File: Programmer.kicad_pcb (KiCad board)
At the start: 2 copper layers, 76.2 x 50.8 mm, 63 parts, among them CON1 USB_OTG, M1 ESP-12E, P1 CONN_01X12, P3 CONN_12, Q1 MMBT3904, Q2 MMBT3906, Q3 MMBT3904, Q4 BSS84, Q5 BSS138L, Q6 MMBT3904, Q7 MMBT3904, SW1 Upload, SW2 RESET, U1 AP2112K-3.3, U10 NC7SB3157, U2 23LC1024, U3 FXMA108, U8 CH340G, Y1 12 Mhz

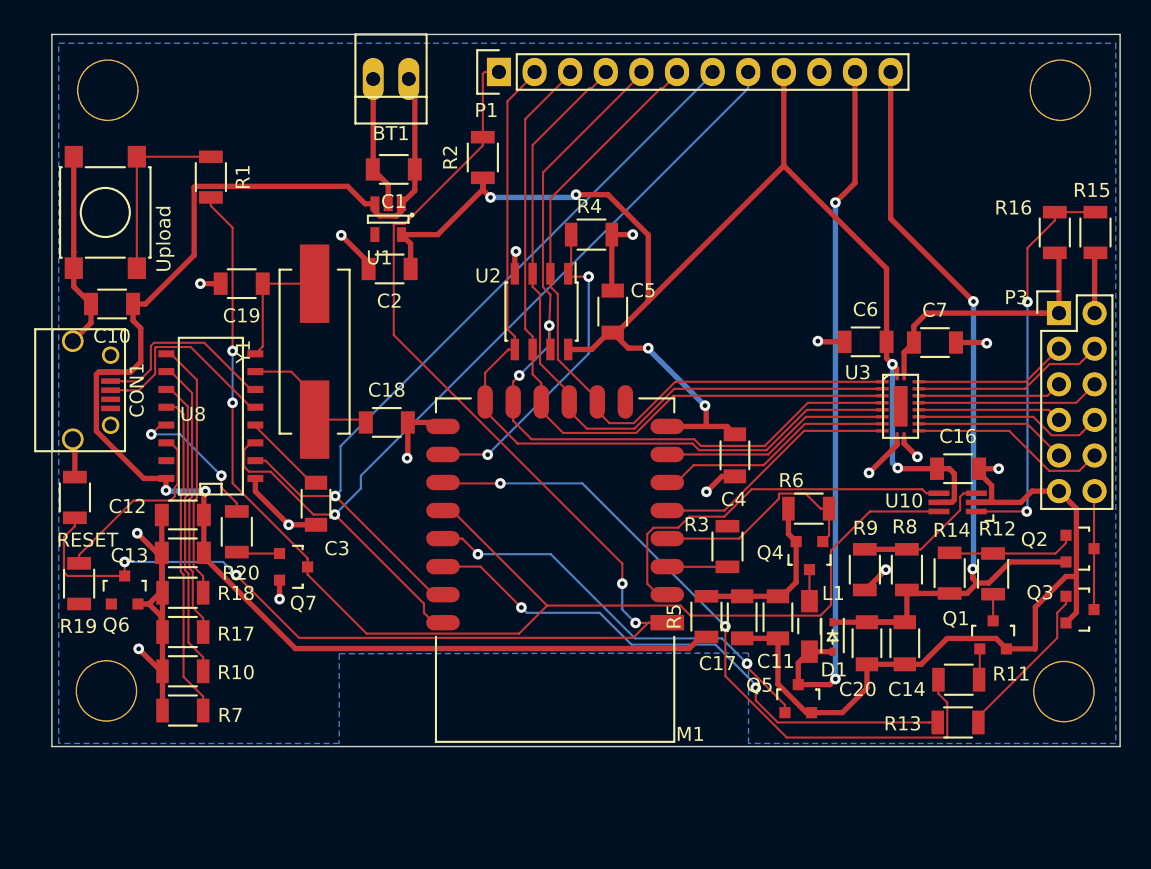
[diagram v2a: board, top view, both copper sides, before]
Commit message: New Layout V00E
Updated layout with newest schematic design.
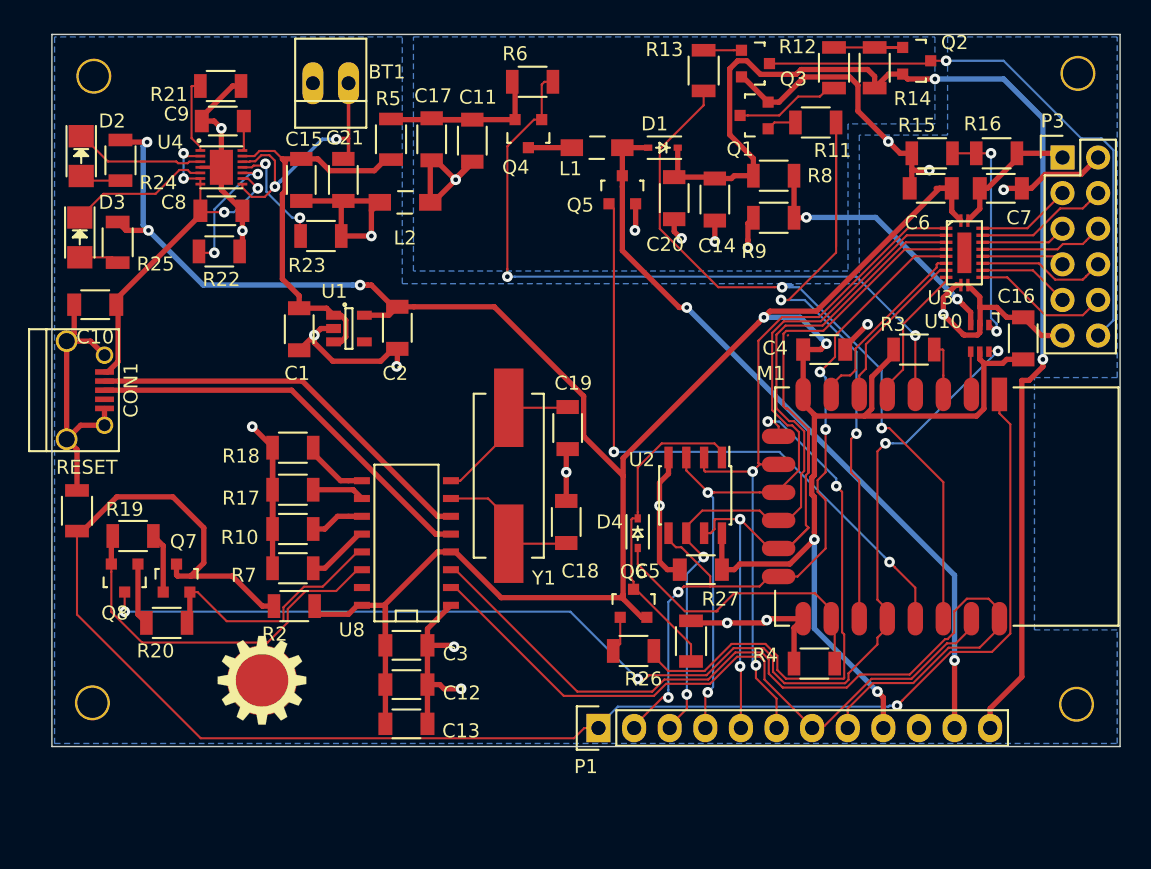
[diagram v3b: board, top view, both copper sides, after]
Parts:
- removed R1: 10K, Resistors_SMD:R_1206
- removed the REF** at (122.8, 40.3)
- removed the REF** at (123.0, 83.2)
- removed the REF** at (54.7, 83.2)
- removed the REF** at (54.8, 40.3)
- removed SW2: RESET, Resistors_SMD:R_1206
- added C15: 1 µF, Capacitors_SMD:C_1206, F.Cu at (68.6, 46.7)
- added C21: 10 µF, Capacitors_SMD:C_1206, F.Cu at (71.6, 46.7)
- added C8: 1 µF, Capacitors_SMD:C_1206, F.Cu at (62.9, 48.9)
- added C9: 0.1 uF, Capacitors_SMD:C_1206, F.Cu at (63.0, 42.5)
- added D2: Red, LEDs:LED_1206, F.Cu at (52.9, 45.0)
- added D3: Green, LEDs:LED_1206, F.Cu at (52.8, 50.8)
- added D4: SD103, Diodes_SMD:SOD-323, F.Cu at (92.6, 71.9)
- added G***: LOGO, UprogrammerFPs:LogoSilk, F.Cu at (65.8, 82.4)
- added G***: LOGO, UprogrammerFPs:LogoMask, F.Cu at (65.8, 82.4)
- added L2: 2.2 µH, Choke_SMD:Choke_SMD_1206_Standard, F.Cu at (76.0, 48.3)
- added Q8: MMBT3904, TO_SOT_Packages_SMD:SOT-23, F.Cu at (56.0, 75.1)
- added R21: 150K, Resistors_SMD:R_1206, F.Cu at (62.9, 40.0)
- added R22: 100K, Resistors_SMD:R_1206, F.Cu at (62.8, 51.8)
- added R23: 10K, Resistors_SMD:R_1206, F.Cu at (70.0, 50.7)
- added R24: 200, Resistors_SMD:R_1206, F.Cu at (55.7, 45.3)
- added R25: 200, Resistors_SMD:R_1206, F.Cu at (55.5, 51.1)
- added R26: 100K, Resistors_SMD:R_1206, F.Cu at (92.3, 80.3)
- added R27: 22K, Resistors_SMD:R_1206, F.Cu at (96.4, 79.6)
- added REF**: MountingHole_2-5mm, Mounting_Holes:MountingHole_2-5mm, F.Cu at (124.0, 39.1)
- added REF**: MountingHole_2-5mm, Mounting_Holes:MountingHole_2-5mm, F.Cu at (123.9, 84.1)
- added REF**: MountingHole_2-5mm, Mounting_Holes:MountingHole_2-5mm, F.Cu at (53.7, 84.0)
- added REF**: MountingHole_2-5mm, Mounting_Holes:MountingHole_2-5mm, F.Cu at (53.8, 39.3)
- added U4: AAT3672-4.2-1, UprogrammerFPs:DFN-14-1EP_3x3mm_Pitch0.4mm, F.Cu at (62.9, 45.9)
- BT1: value BATTERY -> LiPo
- Q1: value MMBT3904 -> BSS138L; footprint Housings_SOT-23_SOT-143_TSOT-6:SOT-23 -> TO_SOT_Packages_SMD:SOT-23
- Q2, Q3, Q4, Q5, Q7: footprint Housings_SOT-23_SOT-143_TSOT-6:SOT-23 -> TO_SOT_Packages_SMD:SOT-23
- Q6: value MMBT3904 -> MMBT3906; footprint Housings_SOT-23_SOT-143_TSOT-6:SOT-23 -> TO_SOT_Packages_SMD:SOT-23
- R4: value 10K -> 22K
- R5: value 10 -> 1K
- R8: value 58.2K -> 100K
- SW1: value Upload -> RESET; footprint Buttons_Switches_SMD:SW_SPST_PTS645 -> Resistors_SMD:R_1206
- U1: footprint Housings_SOT-23_SOT-143_TSOT-6:SOT-23-5 -> TO_SOT_Packages_SMD:SOT-23-5
- U10: footprint Housings_SOT-23_SOT-143_TSOT-6:SC-70-6_Handsoldering -> TO_SOT_Packages_SMD:SC-70-6
- moved R13 49.9 mm to (97.3, 38.9), turned to 270 degrees
- moved P1 47.3 mm to (89.8, 85.8)
- moved Q3 45.3 mm to (101.0, 38.4)
- moved R11 41.0 mm to (105.3, 42.6), turned to 0 degrees
- moved R5 40.8 mm to (75.0, 43.8)
- moved Q1 40.8 mm to (100.9, 42.1), turned to 90 degrees
- moved C17 40.7 mm to (77.9, 43.8)
- moved C11 40.4 mm to (80.8, 43.9)
- moved Q5 38.4 mm to (91.5, 47.4)
- moved R12 37.8 mm to (106.6, 38.7)
- moved L1 37.4 mm to (89.7, 44.4), turned to 0 degrees
- moved D1 36.9 mm to (94.4, 44.4), turned to 180 degrees
- moved Q2 36.7 mm to (112.5, 38.2)
- moved R14 36.4 mm to (109.5, 38.7)
- moved Q6 36.3 mm to (92.3, 76.9)
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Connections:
- BT1 pad 1: +BATT -> Net-(BT1-Pad1)
- C10 pad 1: +BATT -> +5V
- C11 pad 2: GND -> /GNDpp
- C12 pad 1: +BATT -> 3V3
- C13 pad 1: +BATT -> 3V3
- C14 pad 2: GND -> /GNDpp
- C17 pad 2: GND -> /GNDpp
- C20 pad 2: GND -> /GNDpp
- C3 pad 1: Net-(C3-Pad1) -> 3V3
- C5 pad 1: 3V3 -> GND
- C5 pad 2: GND -> 3V3
- CON1 pad 1: +BATT -> +5V
- M1 pad 16: Net-(M1-Pad16) -> /MTDO
- Q5 pad 2: GND -> /GNDpp
- Q6 pad 2: GND -> 3V3
- Q6 pad 3: /~RST -> Net-(D4-Pad1)
- Q7 pad 2: GND -> Net-(Q7-Pad2)
- Q7 pad 3: Net-(M1-Pad18) -> /~RST
- R19 pad 1: Net-(Q6-Pad1) -> Net-(Q7-Pad1)
- R20 pad 1: Net-(Q7-Pad1) -> Net-(Q8-Pad1)
- R20 pad 2: Net-(R20-Pad2) -> Net-(Q7-Pad2)
- R4 pad 2: Net-(M1-Pad16) -> /MTDO
- R9 pad 2: GND -> /GNDpp
- SW1 pad 1: Net-(R1-Pad1) -> GND
- SW1 pad 2: GND -> /~RST
- U2 pad 1: Net-(M1-Pad16) -> Net-(D4-Pad1)
- U8 pad 13: Net-(R20-Pad2) -> Net-(Q7-Pad2)
- U8 pad 16: +BATT -> 3V3
- U8 pad 4: Net-(C3-Pad1) -> 3V3
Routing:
- net 3V3: track 105.4 -> 212.5 mm, vias 6 -> 7
- net +BATT: track 102.5 -> 28.9 mm, vias 2 -> 0
- net Net-(M1-Pad9): track 0.00 -> 39.5 mm, vias 0 -> 2
- net /~HV: track 16.0 -> 51.0 mm, vias 0 -> 2
- net Net-(P3-Pad12): track 8.47 -> 40.9 mm, vias 0 -> 1
- net +5V: track 0.00 -> 27.4 mm, vias 0 -> 4
- net VPP: track 61.7 -> 87.5 mm
- net Net-(M1-Pad2): track 27.5 -> 3.07 mm
- net Net-(D4-Pad1): track 0.00 -> 23.5 mm
- net Net-(M1-Pad16): track 23.3 -> 0.00 mm, vias 2 -> 0
- net /MTDO: track 0.00 -> 21.4 mm
- net Net-(BT1-Pad1): track 0.00 -> 19.9 mm, vias 0 -> 2
- net Net-(R7-Pad2): track 23.3 -> 4.48 mm
- net /GNDpp: track 0.00 -> 18.5 mm, vias 0 -> 5
- net Net-(Q7-Pad2): track 0.00 -> 18.0 mm
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- added copper zone on B.Cu, net /GNDpp

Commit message: Hardware V00F
BOM and Fabrication files
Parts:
- removed G***: LOGO, UprogrammerFPs:LogoSilk
- removed G***: LOGO, UprogrammerFPs:LogoMask
- added Ref**: Val**, UprogrammerFPs:PILogo, F.Cu at (62.9, 83.1)

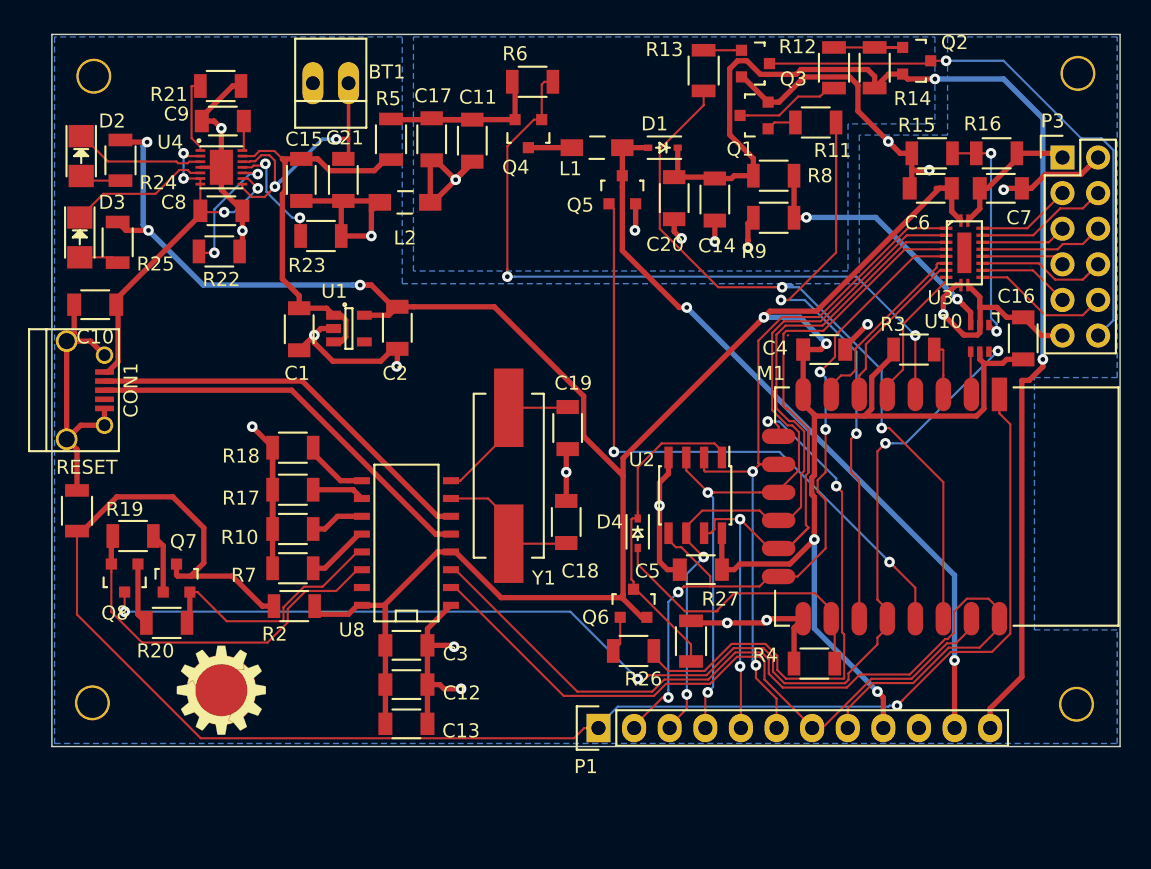
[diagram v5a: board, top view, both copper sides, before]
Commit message: Hardware Version 00H
Schematic updated to get ready for a new layout.
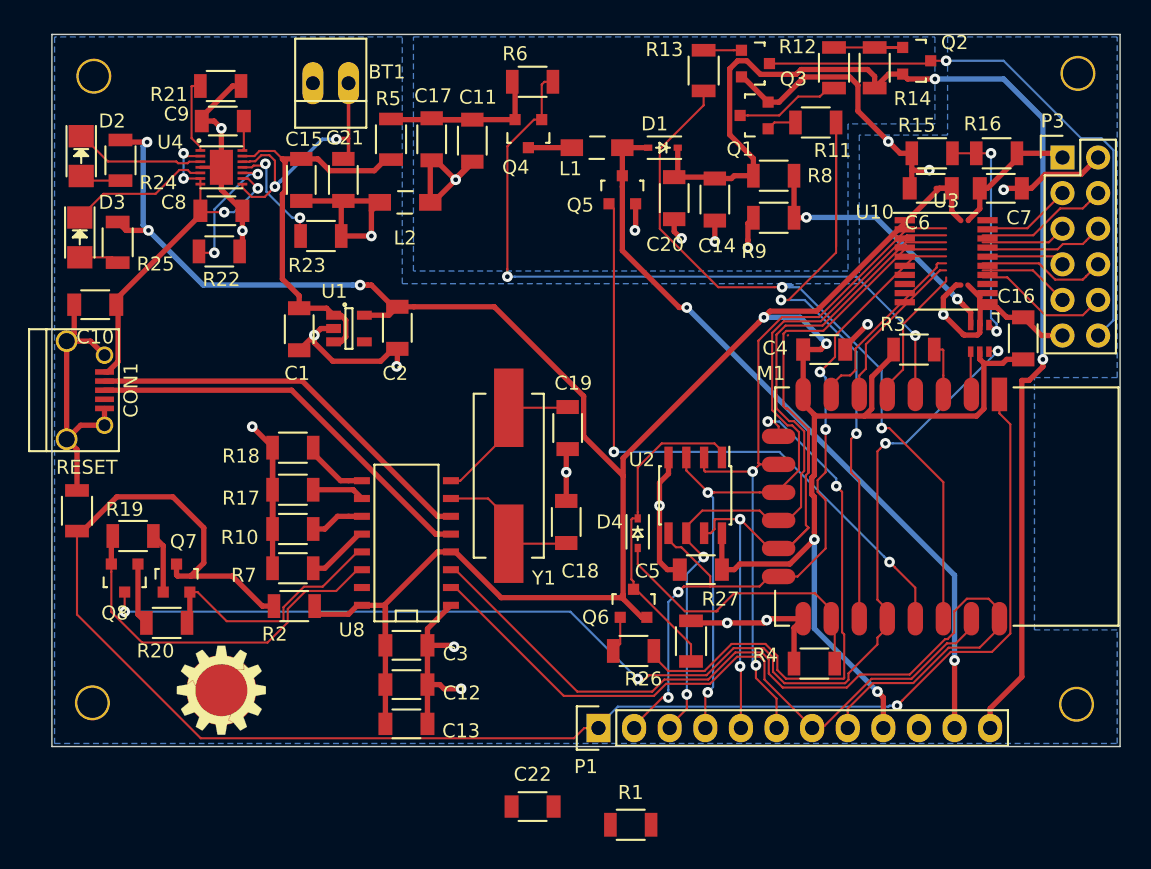
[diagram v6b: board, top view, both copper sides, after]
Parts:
- added C22: 0.1 µF, Capacitors_SMD:C_1206, F.Cu at (85.1, 91.4)
- added R1: 100k, Resistors_SMD:R_1206, F.Cu at (92.1, 92.7)
- R5: value 1K -> 47
- U3: value FXMA108 -> TXS0108EPWR; footprint Uprogrammer FPs:DQFN20 -> Housings_SSOP:TSSOP-20_4.4x6.5mm_Pitch0.65mm
- moved U3 1.43 mm to (114.6, 52.5)
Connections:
- C11 pad 2: /GNDpp -> GND
- C14 pad 2: /GNDpp -> GND
- C17 pad 2: /GNDpp -> GND
- C20 pad 2: /GNDpp -> GND
- CON1 pad 4: Net-(CON1-Pad4) -> (no net)
- D4 pad 2: /MTDO -> (no net)
- M1 pad 11: /IO2 -> /IO3
- M1 pad 12: /SCK -> /IO2
- M1 pad 13: /IO3 -> /MOSI
- M1 pad 14: /MOSI -> /SCLK
- M1 pad 16: /MTDO -> /A_SEL
- P1 pad 3: /SCK -> (no net)
- Q5 pad 2: /GNDpp -> GND
- R4 pad 2: /MTDO -> /A_SEL
- R9 pad 2: /GNDpp -> GND
- U10 pad 6: Net-(M1-Pad18) -> /A_SEL
- U2 pad 1: Net-(D4-Pad1) -> Net-(M1-Pad18)
- U2 pad 6: /SCK -> /SCLK
- U3 pad 1: 3V3 -> /MISO
- U3 pad 10: GND -> Net-(C22-Pad1)
- U3 pad 11: GND -> (no net)
- U3 pad 19: Net-(P3-Pad3) -> VEE
- U3 pad 2: /MISO -> 3V3
- U3 pad 20: VEE -> Net-(P3-Pad3)
- U3 pad 3: /IO2 -> /IO3
- U3 pad 4: /SCK -> /IO2
- U3 pad 5: /IO3 -> /MOSI
- U3 pad 6: /MOSI -> /SCLK
- U8 pad 15: Net-(U8-Pad15) -> (no net)
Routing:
- net /SCK: track 54.1 -> 0.00 mm, vias 2 -> 0
- net /IO2: track 54.7 -> 89.3 mm
- net /SCLK: track 0.00 -> 32.3 mm, vias 0 -> 3
- net /A_SEL: track 0.00 -> 22.1 mm, vias 0 -> 1
- net /MTDO: track 21.4 -> 0.00 mm
- net 3V3: track 212.5 -> 229.2 mm
- net /MISO: track 51.7 -> 35.0 mm
- net GND: track 168.3 -> 181.4 mm, vias 17 -> 22
- net /GNDpp: track 18.5 -> 5.38 mm, vias 5 -> 0
- net /IO3: track 60.4 -> 49.5 mm
- net Net-(D4-Pad1): track 23.5 -> 12.9 mm
- net Net-(M1-Pad18): track 87.6 -> 97.6 mm, vias 4 -> 3
- net Net-(P3-Pad10): track 9.81 -> 1.22 mm
- net Net-(P3-Pad5): track 6.10 -> 13.7 mm
- net VEE: track 9.93 -> 13.1 mm
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
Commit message: New Layout Hardware V00I
Updated layout to match schematic in Version H. Ready to go to
fabrication.
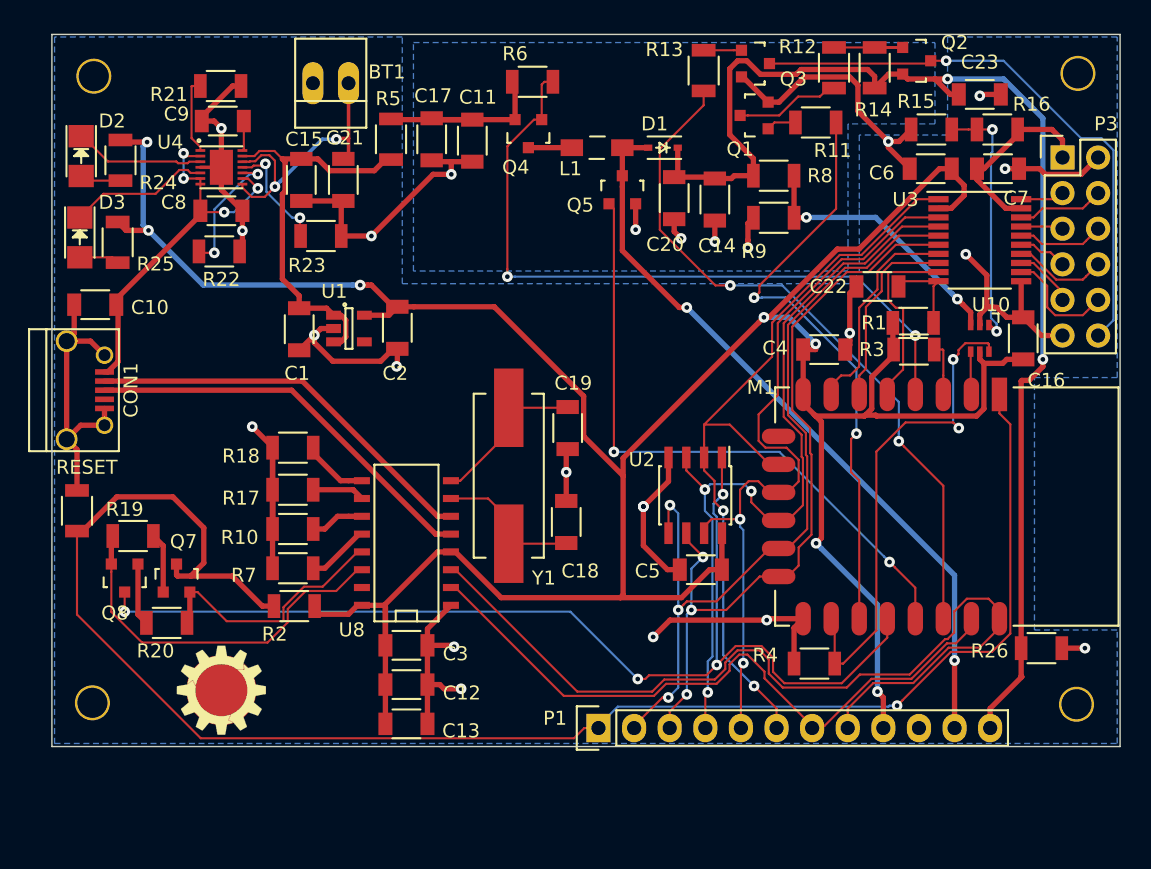
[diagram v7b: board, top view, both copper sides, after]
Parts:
- removed D4: SD103, Diodes_SMD:SOD-323
- removed L2: 2.2 µH, Choke_SMD:Choke_SMD_1206_Standard
- removed Q6: MMBT3906, TO_SOT_Packages_SMD:SOT-23
- removed R27: 22K, Resistors_SMD:R_1206
- added C23: 1 µF, Capacitors_SMD:C_1206, F.Cu at (117.0, 40.6)
- R26: value 100K -> 20K
- U3: value TXS0108EPWR -> TXS0108PWR
- moved C22 44.5 mm to (109.7, 54.3), turned to 180 degrees
- moved R1 41.1 mm to (112.2, 56.9)
- moved R26 29.1 mm to (121.4, 80.1), turned to 0 degrees
- moved U3 2.83 mm to (117.0, 51.0)
- moved R15 1.70 mm to (113.5, 43.1)
- moved R16 1.70 mm to (118.2, 43.1)
- moved C7 1.41 mm to (118.3, 45.9)
- moved C6 1.40 mm to (113.5, 45.9)
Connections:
- M1 pad 9: Net-(M1-Pad9) -> (no net)
- P1 pad 3: (no net) -> /SCLK
- R26 pad 1: Net-(M1-Pad9) -> VPP
- R26 pad 2: Net-(Q6-Pad1) -> GND
- U3 pad 11: (no net) -> GND
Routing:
- net Net-(M1-Pad9): track 39.5 -> 0.00 mm, vias 2 -> 0
- net /IO2: track 89.3 -> 57.5 mm, vias 2 -> 3
- net /SCLK: track 32.3 -> 56.3 mm
- net /MISO: track 35.0 -> 56.2 mm
- net Net-(M1-Pad18): track 97.6 -> 79.5 mm, vias 3 -> 4
- net 3V3: track 229.2 -> 212.9 mm
- net /A_SEL: track 22.1 -> 36.5 mm, vias 1 -> 2
- net Net-(D4-Pad1): track 12.9 -> 0.00 mm
- net Net-(P3-Pad5): track 13.7 -> 3.01 mm
- net /MOSI: track 53.0 -> 60.6 mm
- net GND: track 181.4 -> 188.8 mm, vias 22 -> 24
- net Net-(M1-Pad17): track 49.8 -> 42.6 mm
- net Net-(P3-Pad10): track 1.22 -> 8.11 mm
- net Net-(C22-Pad1): track 0.00 -> 6.55 mm
- net /GNDpp: track 5.38 -> 0.00 mm
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- removed copper zone on B.Cu, net /GNDpp

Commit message: Fixed errors found Hardware V00J
Fixed DTR/RTS Lines and my logo on the board
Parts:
- removed the Ref** at (62.9, 83.1)
- added Ref**: Val**, UprogrammerFPs:PILogo1, F.Cu at (64.1, 83.0)
- moved R19 6.71 mm to (54.6, 78.5), turned to 90 degrees
- moved R2 4.64 mm to (71.6, 80.2), turned to 270 degrees
- moved Q7 4.28 mm to (58.0, 79.0), turned to 90 degrees
- moved R20 3.29 mm to (61.4, 76.0), turned to 270 degrees
- moved Q8 2.10 mm to (58.1, 75.5), turned to 270 degrees
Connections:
- U8 pad 13: Net-(Q7-Pad2) -> Net-(Q8-Pad2)
- U8 pad 14: Net-(Q8-Pad2) -> Net-(Q7-Pad2)
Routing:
- net /~RST: track 120.2 -> 98.5 mm
- net Net-(Q8-Pad2): track 26.9 -> 20.1 mm
- net Net-(M1-Pad18): track 79.5 -> 75.8 mm
- net Net-(Q7-Pad2): track 18.0 -> 15.9 mm
- net 3V3: track 212.9 -> 211.3 mm
